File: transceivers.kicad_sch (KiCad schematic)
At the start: 18 parts, among them U401 TLE9351VSJ, U402 TLE7258SJ

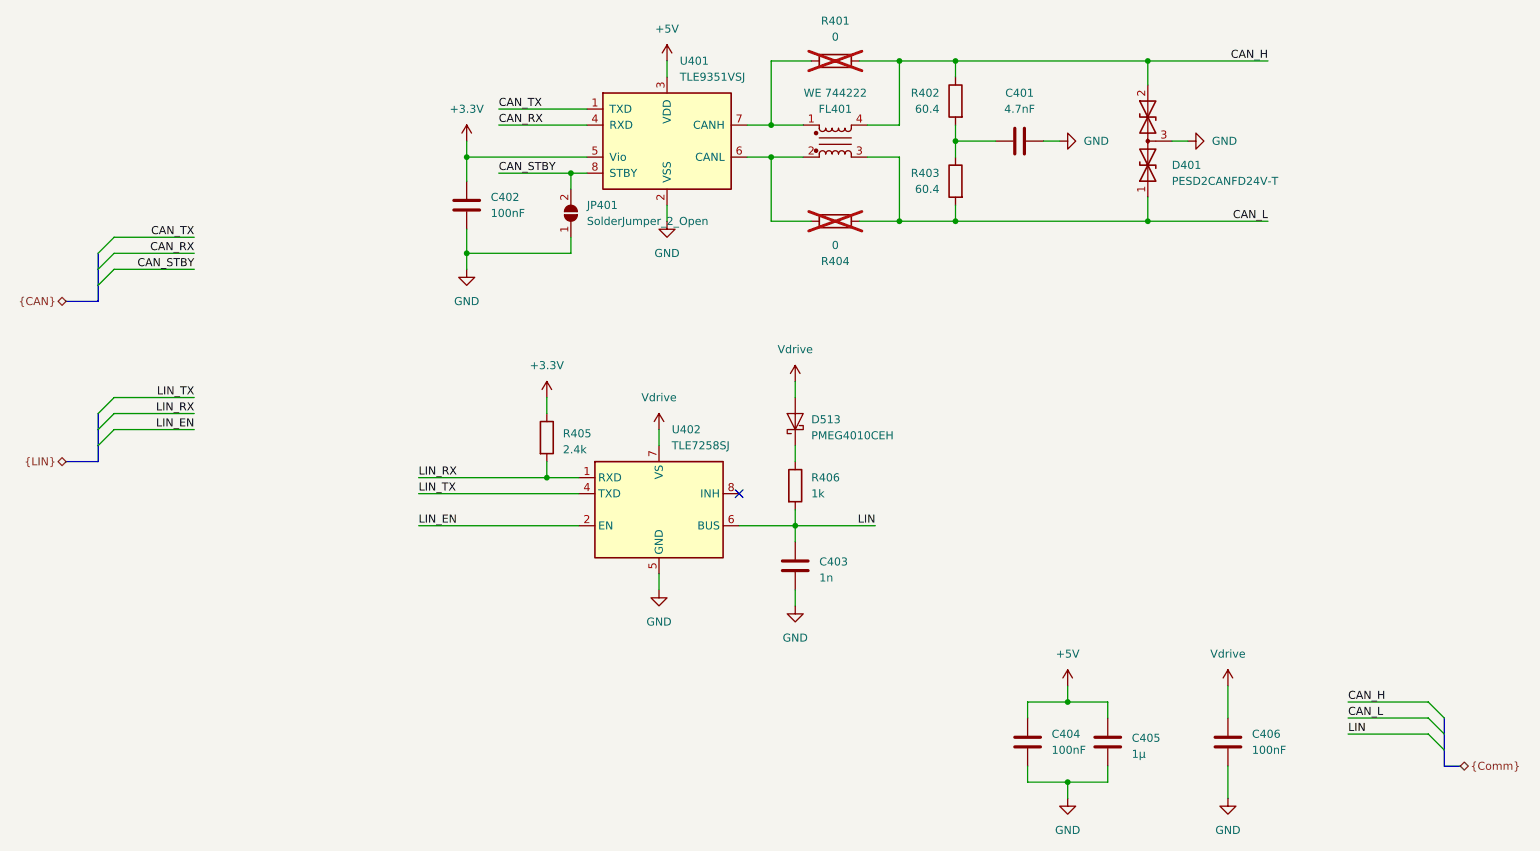
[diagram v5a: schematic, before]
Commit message: hierarchical sheets for digital I/O and replaced power supply jumpers with relays
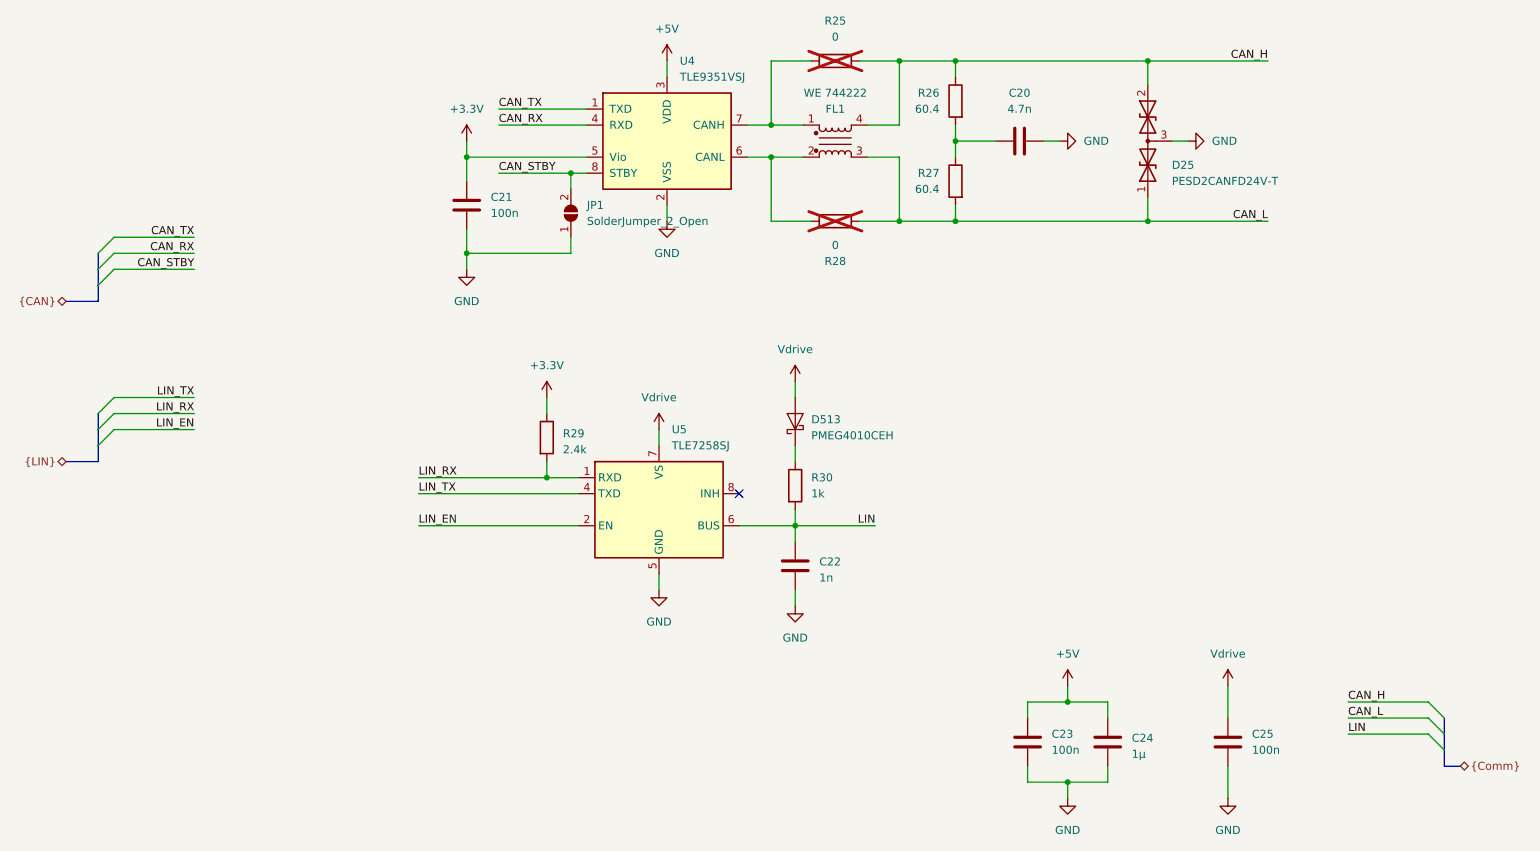
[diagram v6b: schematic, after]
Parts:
- C20: renamed from C401; value 4.7nF -> 4.7n
- C21: renamed from C402; value 100nF -> 100n
- C23: renamed from C404; value 100nF -> 100n
- C25: renamed from C406; value 100nF -> 100n
- renumbered C403 to C22, C405 to C24, D401 to D25, FL401 to FL1, JP401 to JP1, R401 to R25, R402 to R26, R403 to R27, R404 to R28, R405 to R29, R406 to R30, U401 to U4, U402 to U5
